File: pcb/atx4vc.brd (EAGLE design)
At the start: 86 x 70 mm, 67 parts, among them IC2 REG1117, IC3 STM32F042F4, IC4 MY_7905DT, J1 ATX24RH, SW1 324_SW, SW2 324_SW, SW3 324_SW, SW4 324_SW, SW5 324_SW, SW7 324_SW, U1 USBC_16P, U2 USBC_16P

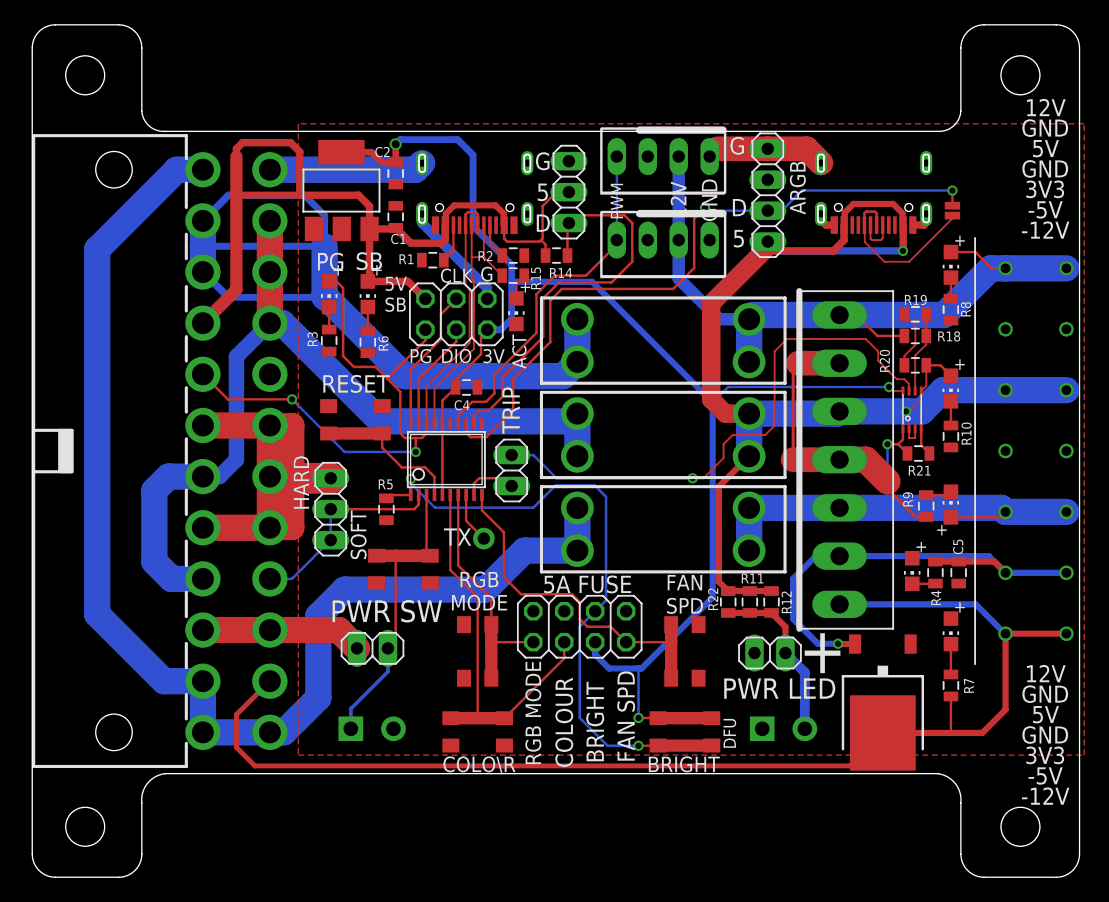
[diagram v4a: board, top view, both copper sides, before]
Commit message: added 5VSB to terminal block, cleaned up files
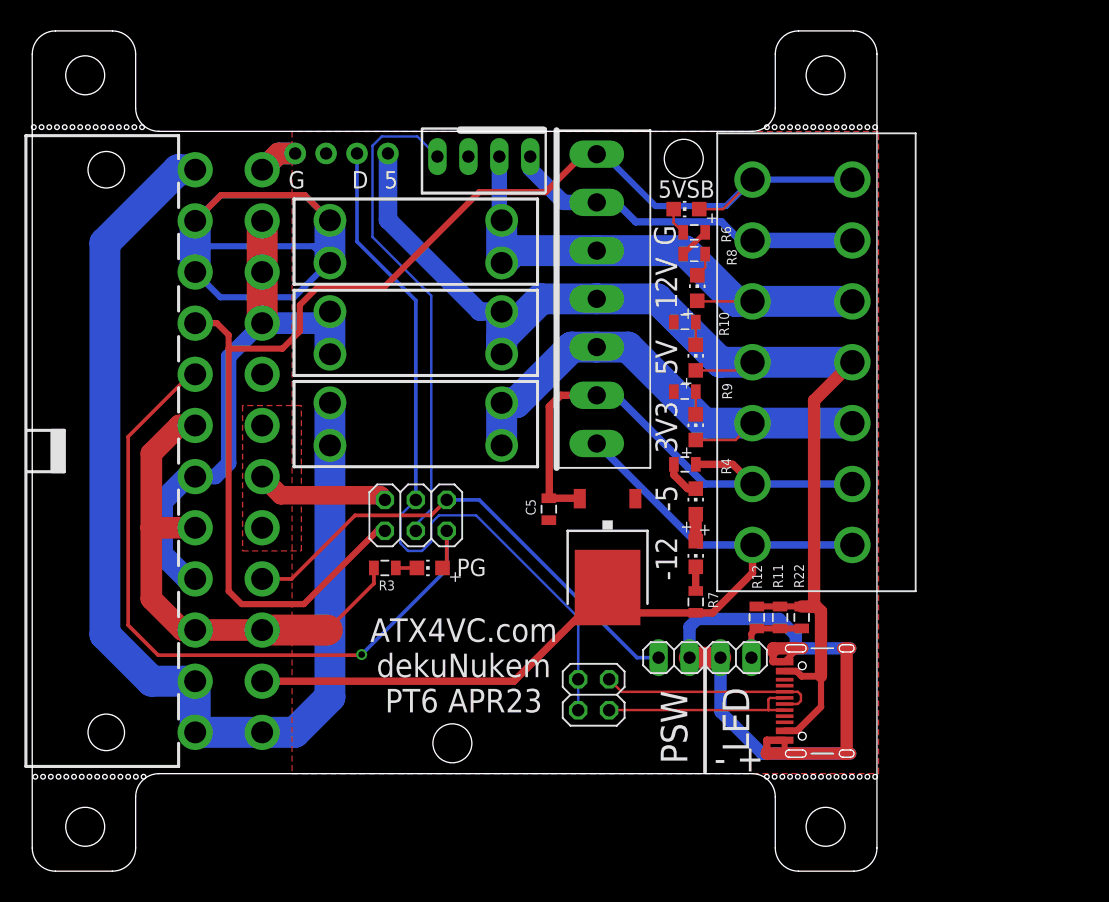
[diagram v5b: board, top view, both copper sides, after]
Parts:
- removed C1, C4: 100nF, atx_power_control:0805$1
- removed C2: 10uF, atx_power_control:0805$1
- removed IC2: REG1117, atx_power_control:SOT223
- removed IC3: STM32F042F4, tx:TSSOP20
- removed J5, J8: (no value), atx_power_control:SCREWTERMINAL-3.5MM-2
- removed JP10: (no value), adafruit:1X01-CLEANBIG
- removed JP11: (no value), pinhead:1X03
- removed JP12: (no value), pinhead:1X04
- removed JP13: JUMPER-SMT_2_NO_NO-SILK, SparkFun-Jumpers:SMT-JUMPER_2_NO_NO-SILK
- removed JP15: (no value), pinhead:2X03
- removed JP16: (no value), appleii:1X04
- removed JP5: (no value), atx_power_control:1X03
- removed JP6: (no value), atx_power_control:1X02
- removed JP9: (no value), atx_power_control:2X04
- removed LED8: (no value), adafruit:CHIP-LED0805
- removed R1, R14, R15, R18, R19, R2, R20, R21, R5: 5K1, atx_power_control:0805
- removed SW1, SW2, SW3, SW4, SW5, SW7: 324_SW, 3pos_slide_switch_centered:342_SWICH_FOOT
- removed U1, U2: USBC_16P, my_usbc_16p:USBC_16P_FOOT
- added J4: (no value), SparkFun-Connectors:USB-C-16P
- added JP2: (no value), pinhead:1X02
- added JP4: (no value), pinhead:2X02
- added U$11: M3_MOUNTING_HOLE, a:M3_MOUNTING_HOLE_PACK
- added U$12: PINHD1X4, adafruit_changed:1X04-CLEANBIG
- J1: device SparkFun-Connectors:ATX24_RIGHT_ANGLE -> nomcu:ATX24_RIGHT_ANGLE
- JP3: device pinhead:1X02 -> pinhead:2X03
- U$6: value 74LVC2G08 -> M3_MOUNTING_HOLE; device atx4vc:VSSOP08 -> a:M3_MOUNTING_HOLE_PACK
- U$9: value WAGO257-7 -> DG2204R-5.0; device atx4vc:WAGO257-7 -> atx4vc:DG2204R
- moved C5 34.1 mm to (42.4, 30.2)
- moved U$6 28.6 mm to (53.5, 59.0)
- moved R6 28.3 mm to (54.4, 53.0), turned to 180 degrees
- moved LED2 27.1 mm to (53.7, 54.9), turned to 90 degrees
- moved IC4 25.6 mm to (47.2, 26.3)
- moved LED3 23.9 mm to (32.6, 25.4), turned to 90 degrees
- moved U$4 23.9 mm to (46.4, 47.5)
- moved R10 23.8 mm to (53.6, 45.6), turned to 0 degrees
- moved R4 22.4 mm to (53.6, 33.9), turned to 180 degrees
- moved U$7 22.1 mm to (31.5, 37.2)
- moved R7 22.1 mm to (54.5, 22.6)
- moved U$8 22.0 mm to (31.5, 44.7)
- moved R9 21.9 mm to (53.6, 39.9), turned to 0 degrees
- moved LED4 21.9 mm to (54.5, 26.5)
- moved LED6 21.9 mm to (54.5, 37.0)
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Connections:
- removed net +3V3: C2.2, C4.2, IC2.2, IC2.4, IC3.16, IC3.5, JP15.5, JP9.4, SW4.P$1, SW4.P$4, U$6.8
- removed net BUTTON1: IC3.4, SW3.P$2, SW3.P$3
- removed net BUTTON2: IC3.1, JP9.3, R5.2, SW4.P$2, SW4.P$3
- removed net F12V_DIV2: R18.2, R19.1, U$6.6
- removed net N$12: U$6.2, U$6.3
- removed net N$13: IC3.6, JP9.6, SW2.P$1, SW2.P$4
- removed net N$19: LED8.A, R15.2
- removed net N$22: IC3.7, JP9.8, SW5.P$1, SW5.P$4
- removed net N$23: IC3.8, JP10.1
- removed net N$24: JP3.2, U$6.7
- removed net N$25: IC3.2, J1.16, JP5.1, JP5.2
- removed net N$26: IC3.3, J5.1, JP6.2, SW1.P$2, SW1.P$3
- removed net N$27: IC3.10, JP9.2, SW7.P$1, SW7.P$4
- removed net N$31: R1.1, U2.B5
- removed net N$33: R2.1, U2.A5
- removed net N$34: JP13.2, U1.A6, U1.B6
- removed net N$35: IC3.13, JP12.2, JP13.1
- removed net N$36: U1.A7, U1.B7
- removed net N$38: IC3.9, JP3.1
- removed net PG: IC3.18, J1.8, JP15.1, LED3.A, U2.A6, U2.B6
- removed net USB_DN: IC3.17, R15.1, U2.A7, U2.B7
- new net N$11: J1.8, JP3.5, LED3.A
- new net N$15: J1.16, JP2.2, JP3.6
- net -12V: now also U$9.P$13, U$9.P$14; no longer U$9.P$1, U$9.P$2
- net -5V: now also U$9.P$11, U$9.P$12; no longer U$9.P$3, U$9.P$4
- net F12V: now also U$4.P$5, U$9.P$5, U$9.P$6; no longer JP16.2, R18.1, U$4.P$7, U$9.P$13, U$9.P$14
- net F3V3: now also U$9.P$10, U$9.P$9; no longer R21.2, U$6.1, U$9.P$5, U$9.P$6
- net F5V: now also J4.VBUS1, J4.VBUS2, U$12.1, U$4.P$4, U$9.P$7, U$9.P$8; no longer JP12.1, R20.1, U$4.P$5, U$6.5, U$9.P$10, U$9.P$9, U1.A4B9, U1.B4A9
- net GND: now also J4.GND, J4.GND2, J4.SHLD1, J4.SHLD2, J4.SHLD3, J4.SHLD4, J4.SHLD5, J4.SHLD6, J4.SHLD7, J4.SHLD8, JP2.1, JP3.2, U$12.4, U$9.P$3, U$9.P$4; no longer C1.1, C2.1, C4.1, IC2.1, IC3.15, J5.2, J8.1, JP11.3, JP12.4, JP15.6, JP16.1, JP5.3, JP6.1, JP9.1, JP9.5, JP9.7, LED8.C, R1.2, R19.2, R2.2, R20.2, R21.1, R5.1, SW1.P$1, SW1.P$4, SW2.P$2, SW2.P$3, SW3.P$1, SW3.P$4, SW5.P$2, SW5.P$3, SW7.P$2, SW7.P$3, U$4.P$4, U$6.4, U$9.P$11, U$9.P$12, U$9.P$7, U$9.P$8, U1.A1B12, U1.B11A12, U1.P$13, U1.P$14, U1.P$15, U1.P$16, U2.A1B12, U2.B11A12, U2.P$13, U2.P$14, U2.P$15, U2.P$16
- net N$17: no longer J8.2
- net N$3: now also JP3.3, JP8.4; no longer IC3.20, JP15.4
- net N$4: now also J4.A6, J4.B6, JP4.2; no longer IC3.19, JP15.3
- net N$6: now also J4.A7, J4.B7, JP4.4; no longer IC3.12, JP11.1, R14.1
- net N$7: now also JP3.4, JP4.1, JP4.3, U$12.2; no longer IC3.14, JP16.4, JP8.4
- net VCC: now also JP3.1, U$4.P$7, U$9.P$1, U$9.P$2; no longer C1.2, IC2.3, JP11.2, JP15.2, R14.2, U2.A4B9, U2.B4A9
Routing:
- net +3V3: track 122.1 -> 0.00 mm, vias 3 -> 0
- net PG: track 67.0 -> 0.00 mm, vias 2 -> 0
- net N$11: track 0.00 -> 59.6 mm, vias 0 -> 1
- net N$35: track 56.5 -> 0.00 mm, vias 2 -> 0
- net BUTTON2: track 52.7 -> 0.00 mm, vias 2 -> 0
- net N$24: track 45.0 -> 0.00 mm, vias 1 -> 0
- net N$15: track 0.00 -> 40.6 mm
- net GND: track 116.5 -> 155.6 mm
- net N$7: track 29.5 -> 62.6 mm
- net VCC: track 74.1 -> 107.1 mm
- net N$13: track 31.9 -> 0.00 mm
- net -12V: track 101.1 -> 72.4 mm
- net N$27: track 28.7 -> 0.00 mm
- net N$3: track 11.8 -> 40.5 mm
- net N$10: track 71.3 -> 45.1 mm
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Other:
- board size 86 x 70 mm -> 69.4 x 69 mm
- board text added: "- +"
- board text added: "-12"
- board text added: "-5"
- board text added: "3V3"
- board text added: "5V"
- board text added: "5VSB"
- board text added: "ATX4VC.com dekuNukem PT6 APR23"
- board text added: "LED"
- board text added: "PSW"
- board text removed: "+"
- board text removed: "12V GND 5V GND 3V3 -5V -12V"
- board text removed: "3V"
- board text removed: "5A FUSE"
- board text removed: "5V SB"
- board text removed: "ACT"
- board text removed: "ARGB"
- board text removed: "ATX4VC.com dekuNukem NOV 2022 PD2"
- board text removed: "BRIGHT"
- board text removed: "CLK"
- board text removed: "COLOUR"
- board text removed: "COLO\R"
- board text removed: "DFU"
- board text removed: "DIO"
- board text removed: "FAN SPD"
- board text removed: "GND"
- board text removed: "HARD"
- board text removed: "PWM"
- board text removed: "PWR LED"
- board text removed: "PWR SW"
- board text removed: "RESET"
- board text removed: "RGB MODE"
- board text removed: "SB"
- board text removed: "SOFT"
- board text removed: "TRIP"
- board text removed: "TX"
